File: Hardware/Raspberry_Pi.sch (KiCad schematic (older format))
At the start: 10 parts, among them J1 M20-9762042, J2 Motor_2, J3 Motor_1

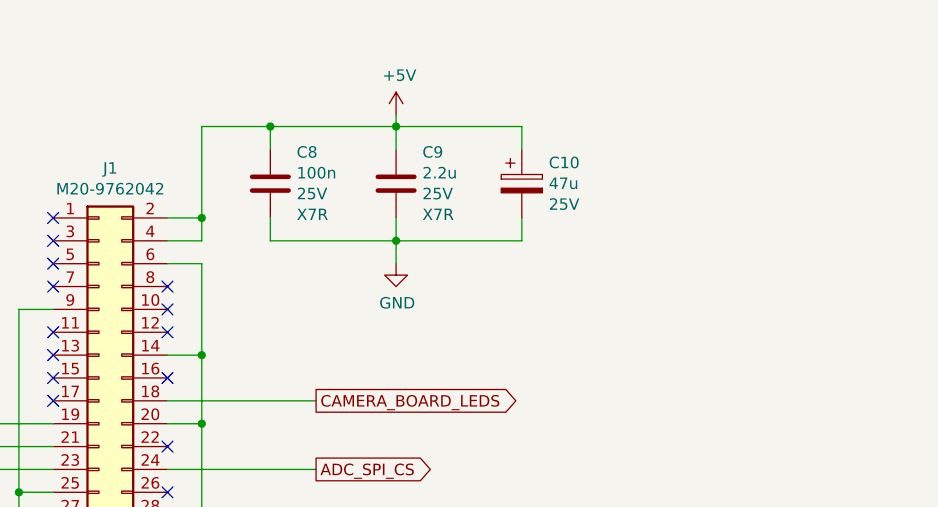
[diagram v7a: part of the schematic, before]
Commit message: [Hardware] Added FTDI cable connector.
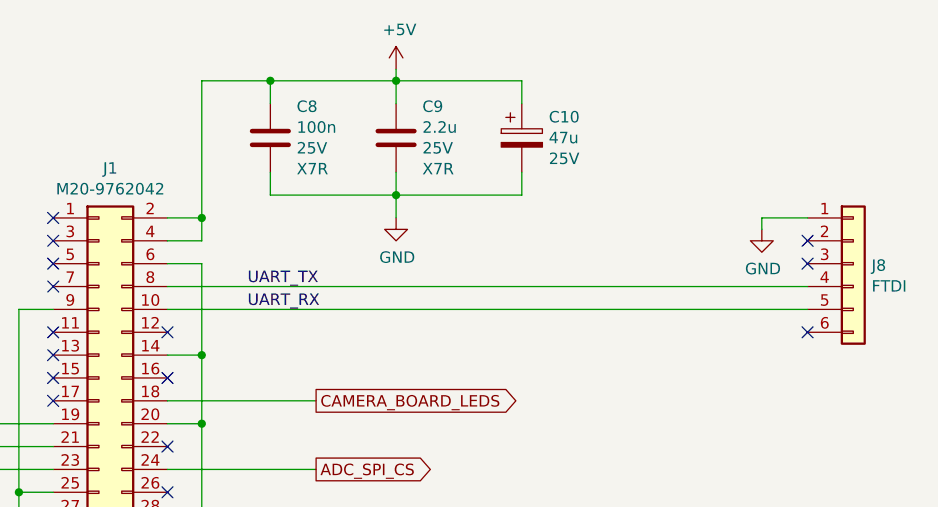
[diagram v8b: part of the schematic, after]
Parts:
- added J8: FTDI, Connector_PinHeader_2.54mm:PinHeader_1x06_P2.54mm_Horizontal, symbol Connector_Generic:Conn_01x06
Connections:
- net GND: now also J8.1 (Pin_1)
- net UART_RX: now reaches J1.10 (Pin_10)
- net UART_RX: now also J8.5 (Pin_5)
- net UART_TX: now reaches J1.8 (Pin_8)
- net UART_TX: now also J8.4 (Pin_4)
- no-connect marks 23 -> 24
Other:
- moved on the sheet: C10, C8, C9
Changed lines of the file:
@@
 L Device:C C?
 U 1 1 5F22CEF4
-P 6150 1900
+P 6150 1700
 AR Path="/5F1F2F9E/5F22CEF4" Ref="C?"  Part="1"
 AR Path="/5F22814A/5F22CEF4" Ref="C8"  Part="1"
-F 0 "C8" H 6035 1763 50  0000 R CNN
-F 1 "100n" H 6035 1854 50  0000 R CNN
-F 2 "Capacitor_SMD:C_1206_3216Metric_Pad1.42x1.75mm_HandSolder" H 6188 1750 50  0001 C CNN
-F 3 "~" H 6150 1900 50  0001 C CNN
-F 4 "25V" H 6035 1945 50  0000 R CNN "Value2"
-F 5 "X7R" H 6035 2036 50  0000 R CNN "Value3"
-	1    6150 1900
+F 0 "C8" H 6035 1563 50  0000 R CNN
+F 1 "100n" H 6035 1654 50  0000 R CNN
+F 2 "Capacitor_SMD:C_1206_3216Metric_Pad1.42x1.75mm_HandSolder" H 6188 1550 50  0001 C CNN
+F 3 "~" H 6150 1700 50  0001 C CNN
+F 4 "25V" H 6035 1745 50  0000 R CNN "Value2"
+F 5 "X7R" H 6035 1836 50  0000 R CNN "Value3"
+	1    6150 1700
 	-1   0    0    1
 $EndComp
@@
 L Device:C C?
 U 1 1 5F22D07D
-P 6700 1900
+P 6700 1700
 AR Path="/5F1F2F9E/5F22D07D" Ref="C?"  Part="1"
 AR Path="/5F22814A/5F22D07D" Ref="C9"  Part="1"
-F 0 "C9" H 6585 1763 50  0000 R CNN
-F 1 "2.2u" H 6585 1854 50  0000 R CNN
-F 2 "Capacitor_SMD:C_1206_3216Metric_Pad1.42x1.75mm_HandSolder" H 6738 1750 50  0001 C CNN
-F 3 "~" H 6700 1900 50  0001 C CNN
-F 4 "25V" H 6585 1945 50  0000 R CNN "Value2"
-F 5 "X7R" H 6585 2036 50  0000 R CNN "Value3"
-	1    6700 1900
+F 0 "C9" H 6585 1563 50  0000 R CNN
+F 1 "2.2u" H 6585 1654 50  0000 R CNN
+F 2 "Capacitor_SMD:C_1206_3216Metric_Pad1.42x1.75mm_HandSolder" H 6738 1550 50  0001 C CNN
+F 3 "~" H 6700 1700 50  0001 C CNN
+F 4 "25V" H 6585 1745 50  0000 R CNN "Value2"
+F 5 "X7R" H 6585 1836 50  0000 R CNN "Value3"
+	1    6700 1700
 	-1   0    0    1
 $EndComp
@@
 L Device:CP C10
 U 1 1 5F22DB67
-P 7250 1900
-F 0 "C10" H 7368 1991 50  0000 L CNN
-F 1 "47u" H 7368 1900 50  0000 L CNN
-F 2 "Capacitor_SMD:CP_Elec_5x5.4" H 7288 1750 50  0001 C CNN
-F 3 "~" H 7250 1900 50  0001 C CNN
-F 4 "25V" H 7368 1809 50  0000 L CNN "Value2"
-F 5 "MCVVT016M470DA1L" H 7250 1900 50  0001 C CNN "Value3"
-	1    7250 1900
+P 7250 1700
+F 0 "C10" H 7368 1791 50  0000 L CNN
+F 1 "47u" H 7368 1700 50  0000 L CNN
+F 2 "Capacitor_SMD:CP_Elec_5x5.4" H 7288 1550 50  0001 C CNN
+F 3 "~" H 7250 1700 50  0001 C CNN
+F 4 "25V" H 7368 1609 50  0000 L CNN "Value2"
+F 5 "MCVVT016M470DA1L" H 7250 1700 50  0001 C CNN "Value3"
+	1    7250 1700
 	1    0    0    -1
 $EndComp
@@
 L power:+5V #PWR05
 U 1 1 5F22EC69
-P 6700 1600
-F 0 "#PWR05" H 6700 1450 50  0001 C CNN
-F 1 "+5V" H 6715 1773 50  0000 C CNN
-F 2 "" H 6700 1600 50  0001 C CNN
-F 3 "" H 6700 1600 50  0001 C CNN
-	1    6700 1600
+P 6700 1400
+F 0 "#PWR05" H 6700 1250 50  0001 C CNN
+F 1 "+5V" H 6715 1573 50  0000 C CNN
+F 2 "" H 6700 1400 50  0001 C CNN
+F 3 "" H 6700 1400 50  0001 C CNN
+	1    6700 1400
 	1    0    0    -1
 $EndComp
@@
 	5850 2150 5850 2050
 Wire Wire Line
-	5850 1650 6150 1650
-Wire Wire Line
-	6150 1650 6150 1750
+	5850 1450 6150 1450
+Wire Wire Line
+	6150 1450 6150 1550
 Wire Wire Line
 	5700 2050 5850 2050
 Connection ~ 5850 2050
 Wire Wire Line
-	5850 2050 5850 1650
-Wire Wire Line
-	6150 1650 6700 1650
-Connection ~ 6150 1650
-Wire Wire Line
-	6700 1650 6700 1750
-Connection ~ 6700 1650
-Wire Wire Line
-	6700 1600 6700 1650
-Wire Wire Line
-	6700 1650 7250 1650
-Wire Wire Line
-	7250 1650 7250 1750
-Wire Wire Line
-	6150 2050 6150 2150
-Wire Wire Line
-	6150 2150 6700 2150
-Wire Wire Line
-	6700 2150 6700 2050
-Wire Wire Line
-	6700 2150 7250 2150
-Wire Wire Line
-	7250 2150 7250 2050
-Connection ~ 6700 2150
+	6150 1450 6700 1450
+Connection ~ 6150 1450
+Wire Wire Line
+	6700 1450 6700 1550
+Connection ~ 6700 1450
+Wire Wire Line
+	6700 1400 6700 1450
+Wire Wire Line
+	6700 1450 7250 1450
+Wire Wire Line
+	7250 1450 7250 1550
+Wire Wire Line
+	6150 1850 6150 1950
+Wire Wire Line
+	6150 1950 6700 1950
+Wire Wire Line
+	6700 1950 6700 1850
+Wire Wire Line
+	6700 1950 7250 1950
+Wire Wire Line
+	7250 1950 7250 1850
+Connection ~ 6700 1950
 $Comp
 L power:GND #PWR06
 U 1 1 5F233893
-P 6700 2250
-F 0 "#PWR06" H 6700 2000 50  0001 C CNN
-F 1 "GND" H 6705 2077 50  0000 C CNN
-F 2 "" H 6700 2250 50  0001 C CNN
-F 3 "" H 6700 2250 50  0001 C CNN
-	1    6700 2250
-	1    0    0    -1
-$EndComp
-Wire Wire Line
-	6700 2250 6700 2150
+P 6700 2050
+F 0 "#PWR06" H 6700 1800 50  0001 C CNN
+F 1 "GND" H 6705 1877 50  0000 C CNN
+F 2 "" H 6700 2050 50  0001 C CNN
+F 3 "" H 6700 2050 50  0001 C CNN
+	1    6700 2050
+	1    0    0    -1
+$EndComp
+Wire Wire Line
+	6700 2050 6700 1950
 $Comp
 L power:GND #PWR08
@@
 Wire Wire Line
 	3750 3650 3750 4100
-Wire Wire Line
-	6350 2850 5700 2850
 Text GLabel 6350 2850 2    50   Output ~ 0
 CAMERA_BOARD_LEDS
@@
 NoConn ~ 5200 2250
 NoConn ~ 5200 2350
-NoConn ~ 5700 2350
-NoConn ~ 5700 2450
 NoConn ~ 5700 2550
 NoConn ~ 5200 2550
@@
 NoConn ~ 5700 3850
 NoConn ~ 5700 3950
+$Comp
+L Connector_Generic:Conn_01x06 J8
+U 1 1 5F38C85B
+P 8700 2250
+F 0 "J8" H 8780 2242 50  0000 L CNN
+F 1 "FTDI" H 8780 2151 50  0000 L CNN
+F 2 "Connector_PinHeader_2.54mm:PinHeader_1x06_P2.54mm_Horizontal" H 8700 2250 50  0001 C CNN
+F 3 "~" H 8700 2250 50  0001 C CNN
+	1    8700 2250
+	1    0    0    -1
+$EndComp
+Wire Wire Line
+	5850 1450 5850 2050
+Wire Wire Line
+	6350 2850 5700 2850
+Wire Wire Line
+	5700 2450 8500 2450
+Wire Wire Line
+	5700 2350 8500 2350
+Text Label 6050 2350 0    50   ~ 0
+UART_TX
+Text Label 6050 2450 0    50   ~ 0
+UART_RX
+NoConn ~ 8500 2550
+NoConn ~ 8500 2250
+NoConn ~ 8500 2150
+$Comp
+L power:GND #PWR019
+U 1 1 5F3A3CEB
+P 8300 2100
+F 0 "#PWR019" H 8300 1850 50  0001 C CNN
+F 1 "GND" H 8305 1927 50  0000 C CNN
+F 2 "" H 8300 2100 50  0001 C CNN
+F 3 "" H 8300 2100 50  0001 C CNN
+	1    8300 2100
+	1    0    0    -1
+$EndComp
+Wire Wire Line
+	8300 2100 8300 2050
+Wire Wire Line
+	8300 2050 8500 2050
 $EndSCHEMATC
